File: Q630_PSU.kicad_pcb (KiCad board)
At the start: 2 copper layers, 99.1 x 50.8 mm, 25 parts, among them J1 ATX PWR, J2 MAC PWR, J3 MAC AUX, J4 FAN1, J5 FAN2, Q1 2N3904, U1 VXO78012

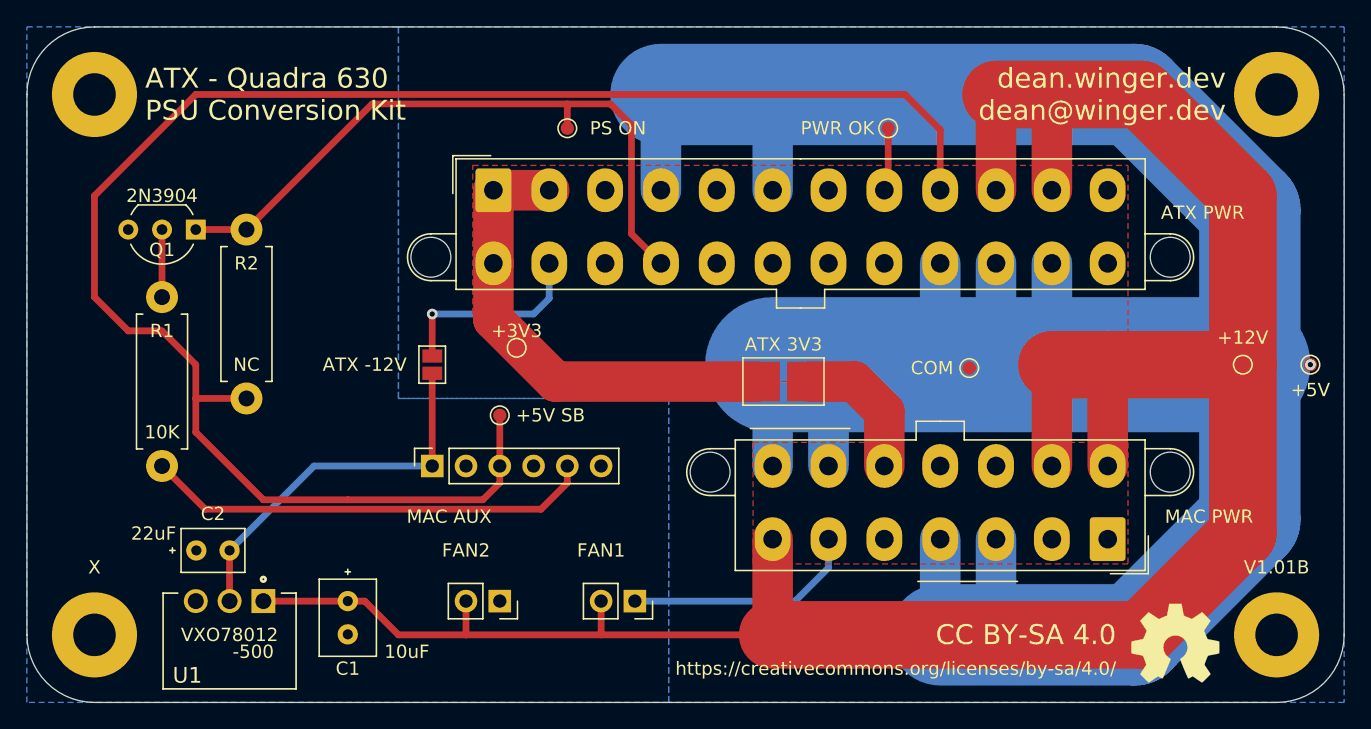
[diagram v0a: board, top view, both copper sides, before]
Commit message: Migrate project to KiCad 6/7 format
Updated PCB and symbol library files to newer KiCad format, added project files and rescue library.
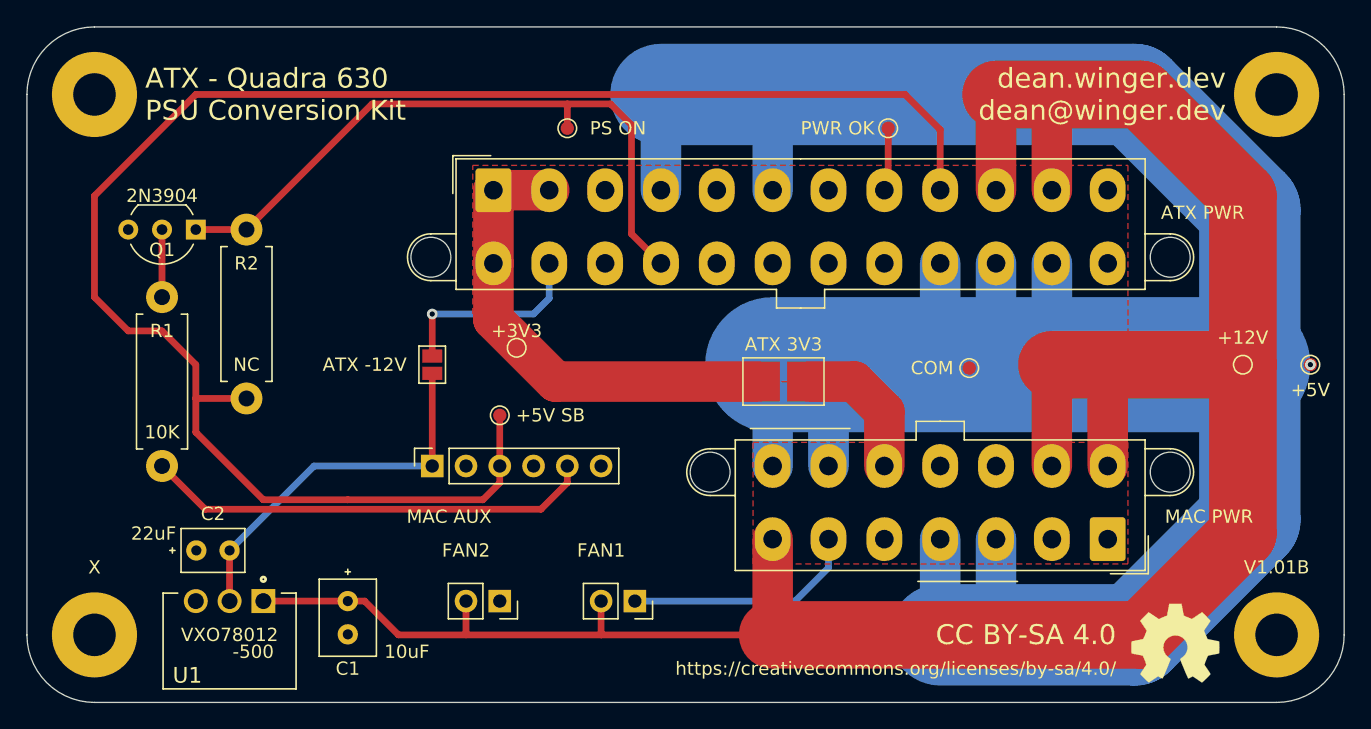
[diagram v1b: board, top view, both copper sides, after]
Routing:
- removed copper zone on B.Cu, net /COM
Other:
- net class Default removed
